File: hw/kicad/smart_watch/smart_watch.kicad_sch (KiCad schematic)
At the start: 7 parts, among them U1 STM32L476RG, U2 GC9A01, U3 LIS2MDL, U4 SHT41

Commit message: block diagram
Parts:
- added C2: 220n, symbol Device:C
- added C3, C5: 100n, symbol Device:C
- added C4: 10u, symbol Device:C
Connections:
- net GND is gone; now on net +3.3V: C1.2, U4.2 (GND)
- net +3.3V: now also U3.6 (GND), U3.8 (GND), C2.1, C3.1, C3.2, C4.1, C4.2, C5.2
- net I2C_SCL: now also U3.1 (SCL)
- net I2C_SDA: now also U3.4 (SDA)
- net +3V3_2: now reaches U3.10 (Vdd_IO)
- net +3V3_2: now also U3.3 (CS), C5.1
- net at U3.5 (C1): now also C2.2
- net LIS2MDL_INT: now reaches U3.7 (INT)

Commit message: work on kicad schematic
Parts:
- removed U1: STM32L476RG, symbol smart_watch:STM32L476RG
- removed U2: GC9A01, symbol smart_watch:GC9A01
- removed U3: LIS2MDL, symbol smart_watch:LIS2MDL
- removed U4: SHT41, symbol smart_watch:SHT41
- added C6: 100n, symbol Device:C
- added C7: 220n, symbol Device:C
- added C8, C9: 10u, symbol Device:C
- added J1: BATTERTY, symbol Connector_Generic:Conn_01x02
- added L1: 200n, symbol Device:L
- added L2: 220n, symbol Device:L
- added R3: 47k, symbol Device:R
- added R4: 250k, symbol Device:R
- added U1: STM32L476RGTx, Package_QFP:LQFP-64_10x10mm_P0.5mm, symbol MCU_ST_STM32L4:STM32L476RGTx
- added U2: nPM1300-QEAA, symbol smart_watch:nPM1300-QEAA
- added U3: SHT41, Sensor_Humidity:Sensirion_DFN-4_1.5x1.5mm_P0.8mm_SHT4x_NoCentralPad, symbol Sensor_Humidity:SHT4x
- added U4: LIS2MDL, Package_LGA:LGA-12_2x2mm_P0.5mm, symbol Sensor_Magnetic:LIS2MDL
- added X5: GC9A01, symbol smart_watch:GC9A01
- C1: value 100n -> 220n
- C2: value 220n -> 100n
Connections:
- net +3V3_2 is gone; now on net +3.3V: C5.1
- net +3.3V: now also C6.2, C9.1, L2.1, U2.32 (VOUT2), U3.3 (VDD), X5.1 (VCC); no longer C1.1, C1.2, C2.1, C3.1, C3.2, C4.1, C4.2, C5.2
- net I2C_SCL: now also U1.61 (PB8), U2.14 (SCL), U3.2 (SCL), U4.1 (SCL/SPC)
- net I2C_SDA: now also U1.62 (PB9), U2.13 (SDA), U3.1 (SDA), U4.4 (SDA/SDI/SDO)
- net GND: now reaches C2.2
- net GND: now also C1.2, C3.2, C4.2, C5.2, C6.1, C7.2, C8.2, C9.2, J1.2 (Pin_2), R3.1, R4.1, U2.18 (NTC), U2.2 (PVSS1), U2.6 (PVSS2), U3.4 (VSS), U4.6 (GND), U4.8 (GND), X5.2 (GND)
- new net: U1.18 (VSS), U1.31 (VSS), U1.47 (VSS), U1.63 (VSS)
- new net: R4.2, U2.16 (VSET2)
- new net: R3.2, U2.17 (VSET1)
- new net: L1.2, U2.3 (SW1)
- new net: L2.2, U2.5 (SW2)
- new net: C1.1, U4.5 (C1)
- new net +1.8V: C3.1, C4.1, C8.1, L1.1, U2.1 (VOUT1), U4.9 (Vdd)
- new net CS: C2.1, U4.10 (Vdd_IO), U4.3 (~{CS})
- new net SPI_CS: U1.58 (PB6), X5.5 (CS), X5.8 (BL)
- new net SPI_DC: U1.43 (PA10), X5.6 (DC)
- new net SPI_MISO: U1.22 (PA6)
- new net SPI_MOSI: U1.23 (PA7), X5.3 (SOA)
- new net SPI_RST: U1.41 (PA8), X5.7 (~{RST})
- new net SPI_SCLK: U1.21 (PA5), X5.4 (SCLK)
- new net VBAT: C7.1, J1.1 (Pin_1), U2.19 (VBAT)
- no-connect marks 0 -> 1
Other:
- note added: "NOTE: R_VSET1 = 47k sets VOUT1 = 1.8V R_VSET2 = 250k sets VOUT2 = 3.3V"

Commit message: schematic
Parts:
- added C10, C15: 100n, symbol Device:C
- added C11: 1u, symbol Device:C
- added C12, C13, C14: 10u, symbol Device:C
- added J2: USB_B_Micro, symbol Connector:USB_B_Micro
- added U5: CH340E, Package_SO:MSOP-10_3x3mm_P0.5mm, symbol Interface_USB:CH340E
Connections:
- net +1.8V: now also U2.12 (VDDIO), C15.1
- net +3.3V: now also U1.1 (VBAT), U1.13 (VDDA), U1.19 (VDD), U1.32 (VDD), U1.48 (VDDUSB), U1.64 (VDD), U2.30 (LSIN2), C10.1, U5.10 (V3), U5.7 (VCC)
- net GND: now also U1.12 (VSSA), U1.18 (VSS), U1.31 (VSS), U1.47 (VSS), U1.63 (VSS), U2.33 (AVSS), C10.2, C11.2, C12.1, C13.1, C14.1, C15.2, J2.5 (GND), U5.3 (GND)
- net USART_TX: now reaches U1.16 (PA2)
- net USART_TX: now also U5.9 (RXD)
- net USART_RX: now reaches U1.17 (PA3)
- net USART_RX: now also U5.8 (TXD)
- net BTN_1: now reaches U1.29 (PB10)
- net BTN_2: now reaches U1.30 (PB11)
- net BOOT0: now reaches U1.60 (BOOT0)
- net NRST: now reaches U1.7 (NRST)
- net LED_1: now reaches U1.8 (PC0)
- net RESET: now reaches U2.15 (SHPHLD)
- net VSYS: now reaches U2.20 (VSYS)
- net VSYS: now also U2.28 (VINLDO1), U2.4 (PVDD), C12.2, C13.2, C14.2
- net VBUS: now reaches U2.21 (VBUS)
- net VBUS: now also J2.1 (VBUS)
- net VBUSOUT: now reaches U2.22 (VBUSOUT)
- net VBUSOUT: now also C11.1
- new net: J2.2 (D-), U5.2 (UD-)
- new net: J2.3 (D+), U5.1 (UD+)
- no-connect marks 1 -> 18
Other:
- moved on the sheet: C1, C2, C3, C4, C5, C6, C7, C8, C9, J1, L1, L2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

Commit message: schematic done?
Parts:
- removed C2, C6: 100n, symbol Device:C
- removed X5: GC9A01, symbol smart_watch:GC9A01
- added C1, C12, C13, C14, C15: 100n, symbol Device:C
- added C10: 4.7u, symbol Device:C
- added C51: 100u, symbol Device:C
- added D1: USBLC6-2SC6, digikey-footprints:SOT23-6L, symbol dk_TVS-Diodes:USBLC6-2SC6
- added J3: GC9A01, symbol Connector_Generic:Conn_01x08
- added J4: JST_ZH6, symbol Connector_Generic:Conn_01x06
- added R1, R10, R11, R12, R2, R3: 10k, symbol Device:R
- added SW1, SW2, SW6: SW_Omron_B3FS, symbol Switch:SW_Omron_B3FS
- C11: value 1u -> 100n
- renumbered C12 to C21, C13 to C22, C14 to C23, C7 to C24, C8 to C25, C9 to C26, C15 to C27, C5 to C30, C4 to C40, C3 to C41, C1 to C42, C10 to C50, L1 to L20, L2 to L21, R3 to R20, R4 to R21, R2 to R30, R1 to R31
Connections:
- net CS is gone; now on net +1.8V: U4.10 (Vdd_IO), U4.3 (~{CS})
- net LED_1 is gone; now on net BTN_1: U1.8 (PC0)
- net RESET is gone; now on net NRST: U2.15 (SHPHLD)
- net +3.3V: now also C11.1, C1.2, C10.1, C12.1, C13.1, C14.1, C15.1, J3.1 (Pin_1), J3.8 (Pin_8), J4.1 (Pin_1), SW1.1, SW2.1, SW6.1
- net BTN_1: now also R1.2, SW2.2; no longer U1.29 (PB10)
- net BTN_2: now also U1.9 (PC1), R2.2, SW1.2; no longer U1.30 (PB11)
- net GND: now also C1.1, C10.2, C12.2, C13.2, C14.2, C15.2, D1.2, J3.2 (Pin_2), J4.2 (Pin_2), R1.1, R10.2, R11.1, R12.2, R2.1, R3.1
- net I2C_SCL: now also R11.2
- net I2C_SDA: now also R12.1
- net NRST: now also C51.2, J4.5 (Pin_5)
- net SPI_CS: now also J3.5 (Pin_5)
- net SPI_DC: now also J3.6 (Pin_6)
- net SPI_MOSI: now also J3.3 (Pin_3)
- net SPI_RST: now also J3.7 (Pin_7)
- net SPI_SCLK: now also J3.4 (Pin_4)
- net VBUS: now also D1.5
- net BTN_3: now reaches U1.10 (PC2)
- net BTN_3: now also R3.2, SW6.2
- net SWDIO: now reaches U1.46 (PA13)
- net SWDIO: now also J4.4 (Pin_4)
- net SWCLK: now reaches U1.49 (PA14)
- net SWCLK: now also J4.3 (Pin_3)
- net at J2.2 (D-): now also D1.3; no longer U5.2 (UD-)
- net at J2.3 (D+): now also D1.1; no longer U5.1 (UD+)
- net at U5.4 (~{RTS}): now also C51.1
- net BOOT0: no longer names the net of U1.60 (BOOT0)
- net BOOT0: now also R10.1
- net SPI_MISO: no longer names the net of U1.22 (PA6)
- net VBAT: no longer names the net of C24.1, J1.1 (Pin_1), U2.19 (VBAT)
- net VBUSOUT: no longer names the net of U2.22 (VBUSOUT)
- net VBUSOUT: no longer C11.1
- new net: D1.4, U5.2 (UD-)
- new net: D1.6, U5.1 (UD+)
- no-connect marks 18 -> 56
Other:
- note added: "Buttons"
- note added: "Decoupling"
- note added: "MCU"
- note added: "Mangnetometer"
- note added: "NOTE: 8 pin FPC connector"
- note added: "Power Management"
- note added: "SWD Header"
- note added: "TFT Display"
- note added: "Temperature-Humidity Sensor"
- note added: "USB Connection"
- moved on the sheet: C21, C22, C23, C24, C25, C26, C27, C30, C40, C41, C42, C50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

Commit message: pmic footprint
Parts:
- U2: footprint (none) -> smart_watch:nPM1300
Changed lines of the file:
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@@
 			)
 		)
-		(property "Footprint" ""
+		(property "Footprint" "smart_watch:nPM1300"
 			(at 142.24 39.37 0)
 			(effects

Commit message: more part selection pt 1
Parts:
- removed J2: USB_B_Micro, symbol Connector:USB_B_Micro
- removed SW1, SW2, SW6: SW_Omron_B3FS, symbol Switch:SW_Omron_B3FS
- added J2: 1051330001, digikey-footprints:USB_Micro_B_Female_Vert_1051330001, symbol dk_USB-DVI-HDMI-Connectors:1051330001
- added SW1, SW2, SW4: SW_Push, Button_Switch_SMD:SW_SPST_TL3305A, symbol Switch:SW_Push
- C1, C10, C11, C12, C13, C14, C15, C21, C22, C23, C24, C25, C26, C27, C30, C40, C41, C42, C50, C51: footprint (none) -> Capacitor_SMD:C_0603_1608Metric
- J1: footprint (none) -> Connector_Molex:Molex_Pico-Lock_205338-0002_1x02-1MP_P2.00mm_Horizontal
- J3: footprint (none) -> Connector_FFC-FPC:Molex_200528-0080_1x08-1MP_P1.00mm_Horizontal
- J4: value JST_ZH6 -> JST_PH6; footprint (none) -> Connector_JST:JST_PH_S6B-PH-K_1x06_P2.00mm_Horizontal
- L20, L21: footprint (none) -> Inductor_SMD:L_0603_1608Metric
- R1, R10, R11, R12, R2, R20, R21, R3, R30, R31: footprint (none) -> Resistor_SMD:R_0603_1608Metric
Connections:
- net +3.3V: now also SW1.1, SW2.1, SW4.1
- net BTN_1: now also SW4.2
- net BTN_2: now also SW1.2
- net BTN_3: now also SW2.2
- net GND: now also J2.5
- net VBUS: now also J2.1
- net at D1.1: now also J2.3
- net at D1.3: now also J2.2

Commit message: start pcb
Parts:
- removed SW1: SW_Push, Button_Switch_SMD:SW_SPST_TL3305A, symbol Switch:SW_Push
- added R4: 10k, Resistor_SMD:R_0603_1608Metric, symbol Device:R
- added SW3, SW4: SW_Push, smart_watch:TL6340, symbol Switch:SW_Push
- SW1: renamed from SW4; footprint Button_Switch_SMD:SW_SPST_TL3305A -> smart_watch:TL6340
- SW2: footprint Button_Switch_SMD:SW_SPST_TL3305A -> smart_watch:TL6340
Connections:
- net +3.3V: now also SW3.1, SW4.1
- net BTN_2: now also SW2.2, U1.26 (PB0); no longer U1.9 (PC1)
- net BTN_3: now also U1.40 (PC9), SW3.2; no longer SW2.2, U1.10 (PC2)
- net GND: now also R4.1
- net BTN_4: now reaches U1.53 (PC12)
- net BTN_4: now also R4.2, SW4.2
- no-connect marks 56 -> 55
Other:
- moved on the sheet: R1, SW1

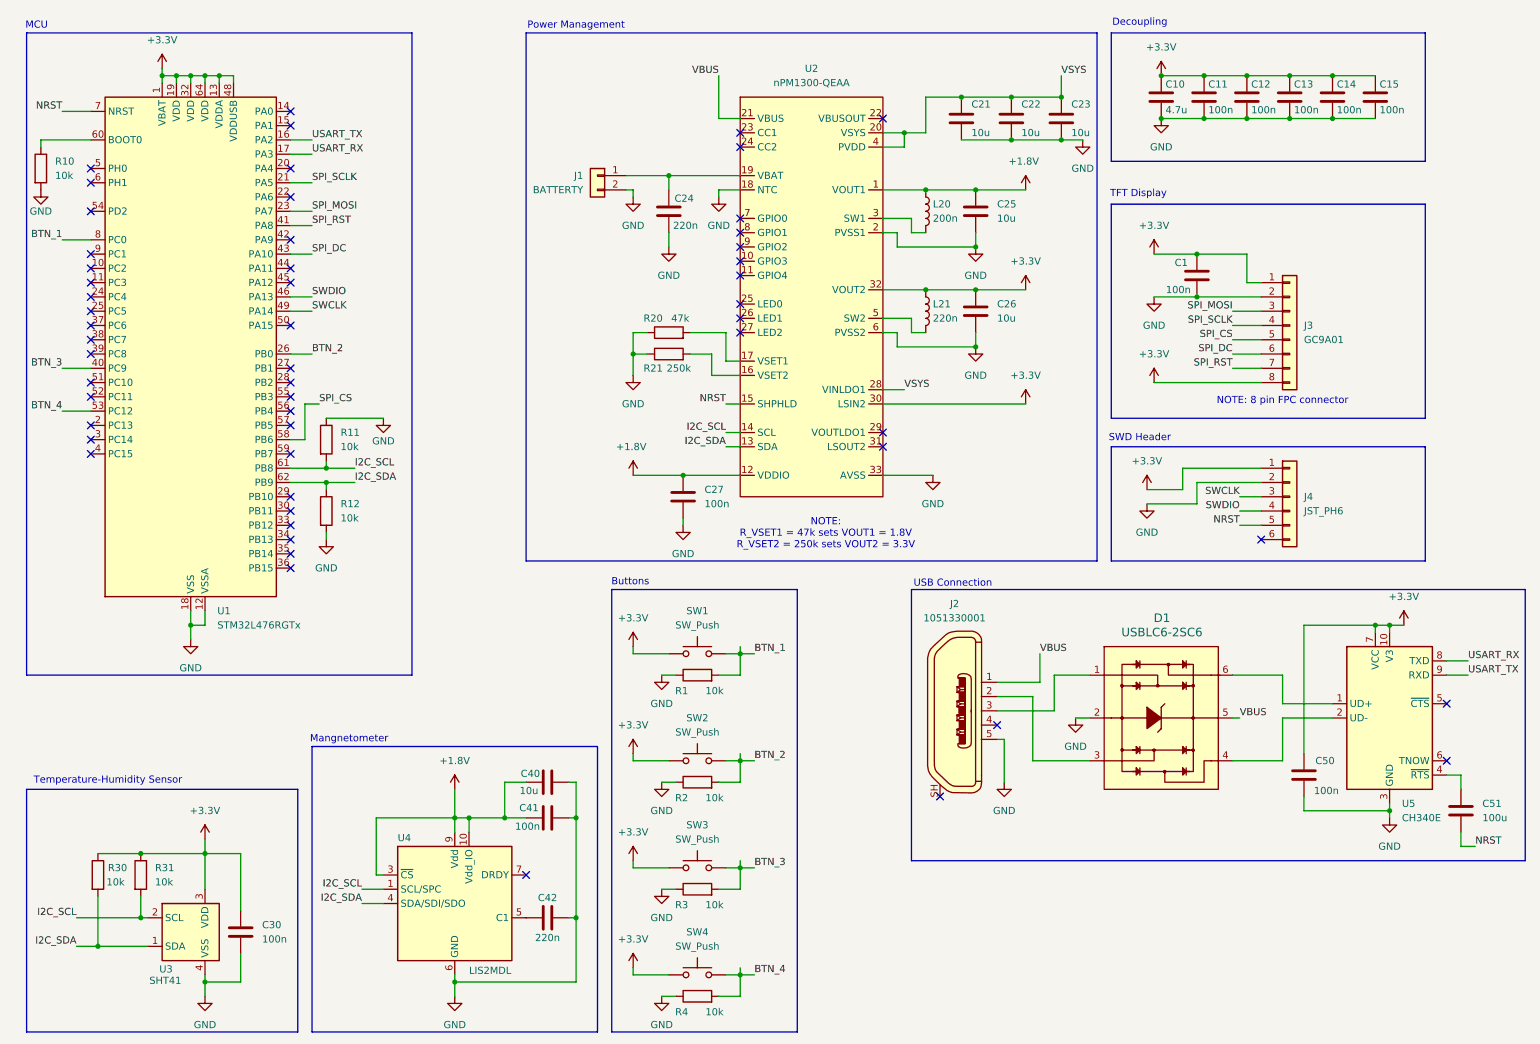
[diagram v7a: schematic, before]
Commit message: added rtc chip to board
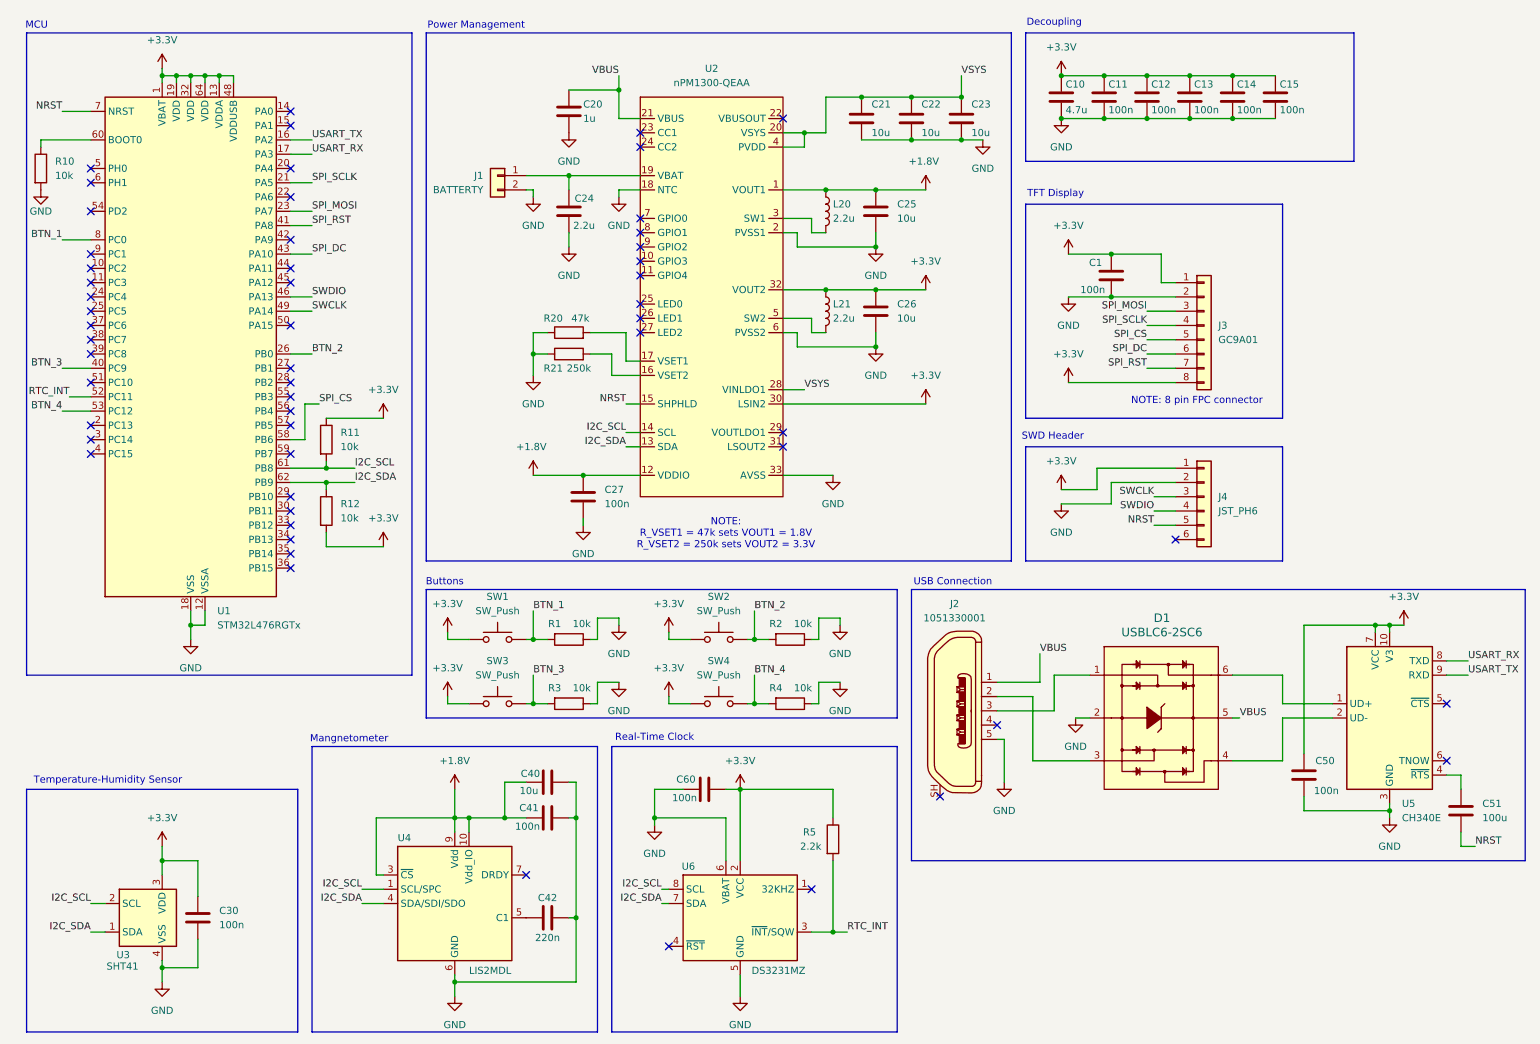
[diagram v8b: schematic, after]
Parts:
- removed R30, R31: 10k, Resistor_SMD:R_0603_1608Metric, symbol Device:R
- added C20: 1u, Capacitor_SMD:C_0201_0603Metric, symbol Device:C
- added C60: 100n, Capacitor_SMD:C_0603_1608Metric, symbol Device:C
- added R5: 2.2k, Resistor_SMD:R_0603_1608Metric, symbol Device:R
- added U6: DS3231MZ, Package_SO:SOIC-8_3.9x4.9mm_P1.27mm, symbol Timer_RTC:DS3231MZ
- C24, L21: value 220n -> 2.2u
- J1: footprint Connector_Molex:Molex_Pico-Lock_205338-0002_1x02-1MP_P2.00mm_Horizontal -> Connector_Molex:Molex_PicoBlade_53261-0271_1x02-1MP_P1.25mm_Horizontal
- L20: value 200n -> 2.2u
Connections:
- net +3.3V: now also R11.1, R12.2, C60.2, R5.1, U6.2 (VCC)
- net GND: now also C20.2, C60.1, U6.5 (GND), U6.6 (VBAT); no longer R11.1, R12.2
- net I2C_SCL: now also U6.8 (SCL)
- net I2C_SDA: now also U6.7 (SDA)
- net VBUS: now also C20.1
- net RTC_INT: now reaches U1.52 (PC11)
- net RTC_INT: now also R5.2, U6.3 (~{INT}/SQW)
- no-connect marks 55 -> 56
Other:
- note added: "Real-Time Clock"
- title: (none) -> Smart Watch
- moved on the sheet: C1, C10, C11, C12, C13, C14, C21, C22, C23, C24, C25, C26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
